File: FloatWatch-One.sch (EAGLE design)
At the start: 51 parts, among them Q1 S8050, Q2 S8050, U1 ATMEGA168P-QFN32, U2 ADXL345, U3 MCP6001-SOT23, U4 APDS-9008, U5 TP4055, U6 3.3V, U7 CH340E, Y1 7.3728MHz

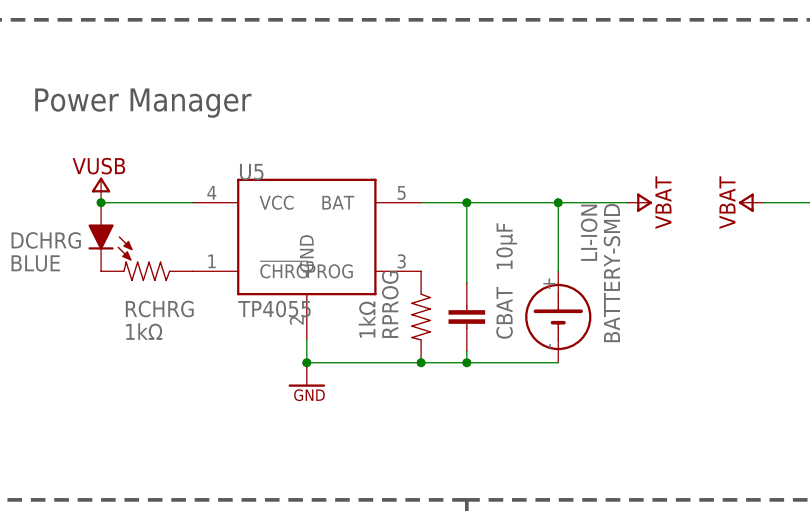
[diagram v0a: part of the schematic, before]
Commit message: Fixes TP4055 footprint bug
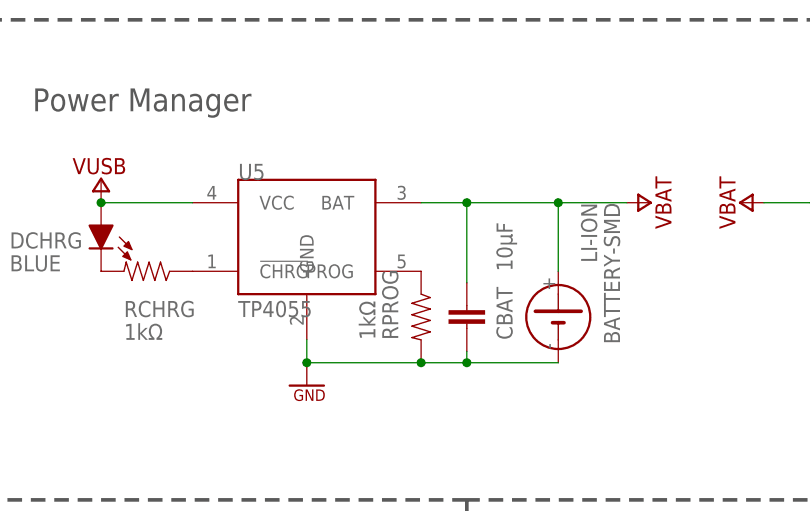
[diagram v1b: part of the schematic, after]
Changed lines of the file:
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@@
 <?xml version="1.0" encoding="utf-8"?>
 <!DOCTYPE eagle SYSTEM "eagle.dtd">
-<eagle version="7.7.0">
+<eagle version="7.6.0">
 <drawing>
 <settings>

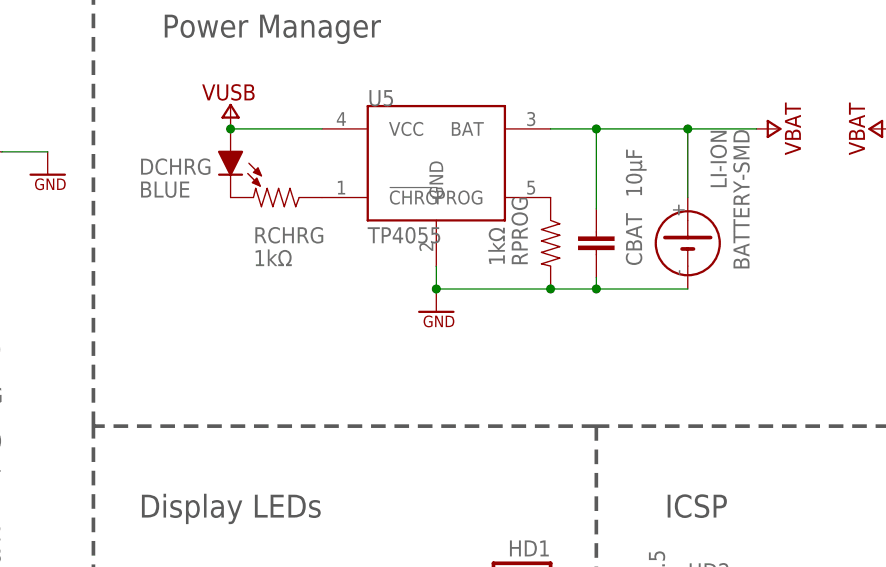
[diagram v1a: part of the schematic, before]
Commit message: Fixes RPROG resistance
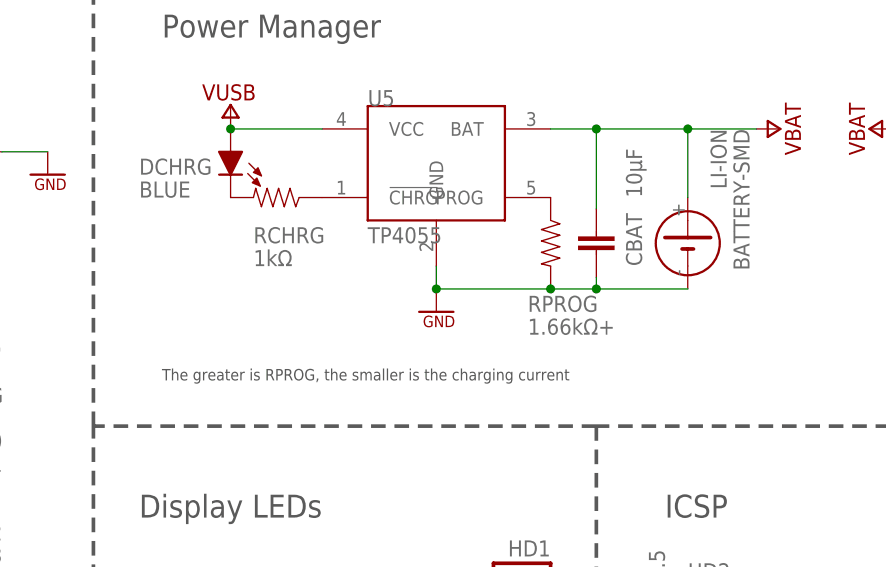
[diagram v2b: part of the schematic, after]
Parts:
- RPROG: value 1kΩ -> 1.66kΩ+
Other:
- note added: "The greater is RPROG, the smaller is the charging current"
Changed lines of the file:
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@@
 <?xml version="1.0" encoding="utf-8"?>
 <!DOCTYPE eagle SYSTEM "eagle.dtd">
-<eagle version="7.6.0">
+<eagle version="7.7.0">
 <drawing>
 <settings>
@@
 <part name="LI-ION" library="MyLibrary" deviceset="BATTERY" device="-SMD" value="BATTERY-SMD"/>
 <part name="SUPPLY17" library="MyLibrary" deviceset="GND" device=""/>
-<part name="RPROG" library="MyLibrary" deviceset="RES" device="-0603" value="1kΩ"/>
+<part name="RPROG" library="MyLibrary" deviceset="RES" device="-0603" value="1.66kΩ+"/>
 <part name="SUPPLY20" library="MyLibrary" deviceset="VBAT" device=""/>
 <part name="SUPPLY21" library="MyLibrary" deviceset="VBAT" device=""/>
@@
 <text x="187.96" y="50.8" size="2.54" layer="97" font="vector">Display LEDs</text>
 <wire x1="182.88" y1="60.96" x2="182.88" y2="7.62" width="0.4064" layer="97" style="longdash"/>
+<text x="63.5" y="12.7" size="1.27" layer="97" font="vector">The greater is RPROG, the smaller is the charging current</text>
 </plain>
 <instances>
@@
 <instance part="SUPPLY17" gate="GND" x="93.98" y="20.32"/>
 <instance part="RPROG" gate="A" x="106.68" y="27.94" smashed="yes" rot="R90">
-<attribute name="NAME" x="104.14" y="25.4" size="1.778" layer="95" rot="R90"/>
-<attribute name="VALUE" x="101.6" y="25.4" size="1.778" layer="96" rot="R90"/>
+<attribute name="NAME" x="104.14" y="20.32" size="1.778" layer="95"/>
+<attribute name="VALUE" x="104.14" y="17.78" size="1.778" layer="96"/>
 </instance>
 <instance part="SUPPLY20" gate="VBAT" x="132.08" y="40.64" rot="R270"/>
